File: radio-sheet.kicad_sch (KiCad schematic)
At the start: 41 parts, among them Q2 AO3401A, Q3 MMBT3904, Q4 AO3401A, U15 74HC04, U5 Si4463, Y4 30M

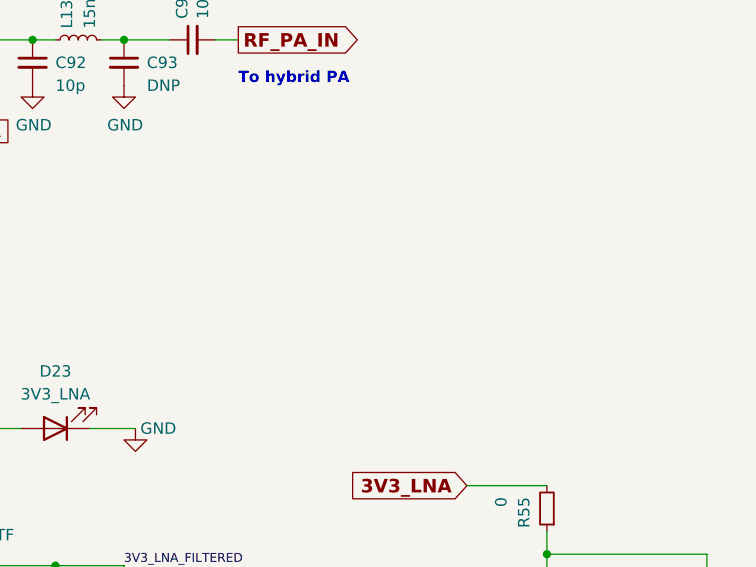
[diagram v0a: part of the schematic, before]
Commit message: added LNA led, adjusted LED resistor for 12V output
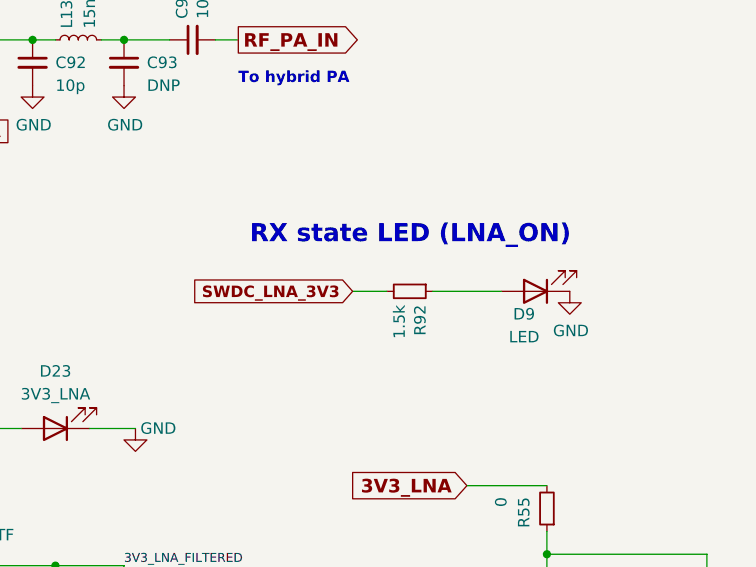
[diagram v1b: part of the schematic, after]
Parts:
- added D9: LED, LED_SMD:LED_0603_1608Metric, symbol Device:LED
- added R92: 1.5k, Resistor_SMD:R_0603_1608Metric, symbol Device:R_Small
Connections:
- net GND: now also D9.1 (K)
- net SWDC_LNA_3V3: now also R92.2
- new net: D9.2 (A), R92.1
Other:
- note added: "RX state LED (LNA_ON)"
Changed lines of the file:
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@@
+    (stroke (width 0) (type default))
+  )
+  (wire (pts (xy 224.79 80.01) (xy 228.6 80.01))
     (stroke (width 0) (type default))
   )
@@
   )
   (wire (pts (xy 165.1 62.23) (xy 168.91 62.23))
+    (stroke (width 0) (type default))
+  )
+  (wire (pts (xy 233.68 80.01) (xy 241.3 80.01))
     (stroke (width 0) (type default))
   )
@@
   (text "RX_STATE" (at 161.29 76.2 0)
     (effects (font (size 1.016 1.016) (thickness 0.2032) bold) (justify left bottom))
+  )
+  (text "RX state LED (LNA_ON)" (at 213.36 74.93 0)
+    (effects (font (size 2.0038 2.0038) (thickness 0.4008) bold) (justify left bottom))
   )
   (text "To hybrid PA" (at 212.09 57.15 0)
@@
     (property "Intersheetrefs" "${INTERSHEET_REFS}" (at 75.0256 111.633 0)
       (effects (font (size 1.27 1.27) (thickness 0.254) bold) (justify left) hide)
+    )
+  )
+  (global_label "SWDC_LNA_3V3" (shape input) (at 224.79 80.01 180) (fields_autoplaced)
+    (effects (font (size 1.27 1.27) (thickness 0.254) bold) (justify right))
+    (property "Intersheetrefs" "${INTERSHEET_REFS}" (at 208.1844 79.883 0)
+      (effects (font (size 1.27 1.27) (thickness 0.254) bold) (justify right) hide)
     )
   )
@@
         )
       )
+    )
+  )
+  (symbol (lib_id "power:GND") (at 248.92 80.01 0) (unit 1)
+    (in_bom yes) (on_board yes) (dnp no)
+    (property "Reference" "#PWR01" (at 248.92 86.36 0)
+      (effects (font (size 1.27 1.27)) hide)
+    )
+    (property "Value" "GND" (at 249.047 84.4042 0)
+      (effects (font (size 1.27 1.27)))
+    )
+    (property "Footprint" "" (at 248.92 80.01 0)
+      (effects (font (size 1.27 1.27)) hide)
+    )
+    (property "Datasheet" "" (at 248.92 80.01 0)
+      (effects (font (size 1.27 1.27)) hide)
+    )
+    (pin "1")
+    (instances
+      (project "TACNPR"
+        (path "/9538e4ed-27e6-4c37-b989-9859dc0d49e8/00000000-0000-0000-0000-00006096f497"
+          (reference "#PWR01") (unit 1)
+        )
+        (path "/9538e4ed-27e6-4c37-b989-9859dc0d49e8/00000000-0000-0000-0000-0000607946f5"
+          (reference "#PWR01") (unit 1)
+        )
+      )
+    )
+  )
+  (symbol (lib_id "Device:LED") (at 245.11 80.01 180) (unit 1)
+    (in_bom yes) (on_board yes) (dnp no)
+    (property "Reference" "D9" (at 243.84 82.55 0)
+      (effects (font (size 1.27 1.27)))
+    )
+    (property "Value" "LED" (at 243.84 85.09 0)
+      (effects (font (size 1.27 1.27)))
+    )
+    (property "Footprint" "LED_SMD:LED_0603_1608Metric" (at 245.11 80.01 0)
+      (effects (font (size 1.27 1.27)) hide)
+    )
+    (property "Datasheet" "~" (at 245.11 80.01 0)
+      (effects (font (size 1.27 1.27)) hide)
+    )
+    (property "LCSC" "C72043" (at 245.11 80.01 0)
+      (effects (font (size 1.27 1.27)) hide)
+    )
+    (pin "1")
+    (pin "2")
+    (instances
+      (project "TACNPR"
+        (path "/9538e4ed-27e6-4c37-b989-9859dc0d49e8/00000000-0000-0000-0000-00006096f497"
+          (reference "D9") (unit 1)
+        )
+        (path "/9538e4ed-27e6-4c37-b989-9859dc0d49e8/00000000-0000-0000-0000-0000607946f5"
+          (reference "D9") (unit 1)
+        )
+      )
+    )
+  )
+  (symbol (lib_id "Device:R_Small") (at 231.14 80.01 270) (unit 1)
+    (in_bom yes) (on_board yes) (dnp no)
+    (property "Reference" "R92" (at 232.3084 81.5086 0)
+      (effects (font (size 1.27 1.27)) (justify left))
+    )
+    (property "Value" "1.5k" (at 229.997 81.5086 0)
+      (effects (font (size 1.27 1.27)) (justify left))
+    )
+    (property "Footprint" "Resistor_SMD:R_0603_1608Metric" (at 231.14 80.01 0)
+      (effects (font (size 1.27 1.27)) hide)
+    )
+    (property "Datasheet" "~" (at 231.14 80.01 0)
+      (effects (font (size 1.27 1.27)) hide)
+    )
+    (property "LCSC" "C118397" (at 231.14 80.01 0)
+      (effects (font (size 1.27 1.27)) hide)
+    )
+    (pin "1")
+    (pin "2")
+    (instances
+      (project "TACNPR"
+        (path "/9538e4ed-27e6-4c37-b989-9859dc0d49e8/00000000-0000-0000-0000-00006096f497"
+          (reference "R92") (unit 1)
+        )
+        (path "/9538e4ed-27e6-4c37-b989-9859dc0d49e8/00000000-0000-0000-0000-0000607946f5"
+          (reference "R92") (unit 1)
+        )
+      )

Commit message: leds to be 0805, also TX (red) -- silk adjustments
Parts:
- D19: footprint LED_SMD:LED_0603_1608Metric -> LED_SMD:LED_0805_2012Metric; LCSC C2286 -> C84256
- D23, D9: footprint LED_SMD:LED_0603_1608Metric -> LED_SMD:LED_0805_2012Metric; LCSC C72043 -> C2297
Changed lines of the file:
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@@
 			)
 		)
-		(property "Footprint" "LED_SMD:LED_0603_1608Metric"
+		(property "Footprint" "LED_SMD:LED_0805_2012Metric"
 			(at 60.96 134.62 0)
 			(effects
@@
 			)
 		)
-		(property "LCSC" "C2286"
+		(property "LCSC" "C84256"
 			(at 60.96 134.62 0)
 			(effects
@@
 			)
 		)
-		(property "Footprint" "LED_SMD:LED_0603_1608Metric"
+		(property "Footprint" "LED_SMD:LED_0805_2012Metric"
 			(at 191.77 95.25 0)
 			(effects
@@
 			)
 		)
-		(property "LCSC" "C72043"
+		(property "LCSC" "C2297"
 			(at 191.77 95.25 0)
 			(effects
@@
 			)
 		)
-		(property "Footprint" "LED_SMD:LED_0603_1608Metric"
+		(property "Footprint" "LED_SMD:LED_0805_2012Metric"
 			(at 245.11 80.01 0)
 			(effects
@@
 			)
 		)
-		(property "LCSC" "C72043"
+		(property "LCSC" "C2297"
 			(at 245.11 80.01 0)
 			(effects

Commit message: si4463 lcsc code
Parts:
- U5: DNP TRUE -> (none); LCSC (none) -> C476202
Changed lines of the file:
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@@
 	(label "3V3_LNA_FILTERED"
 		(at 199.39 110.49 0)
-		(fields_autoplaced yes)
 		(effects
 			(font
@@
 			)
 		)
-		(property "DNP" "TRUE"
+		(property "LCSC" "C476202"
 			(at 124.46 64.77 0)
 			(effects
 				(font
-					(size 1.27 1.27)
-				)
-				(hide yes)
+					(size 5.0038 5.0038)
+				)
+				(hide yes)
